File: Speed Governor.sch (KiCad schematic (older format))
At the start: 11 parts

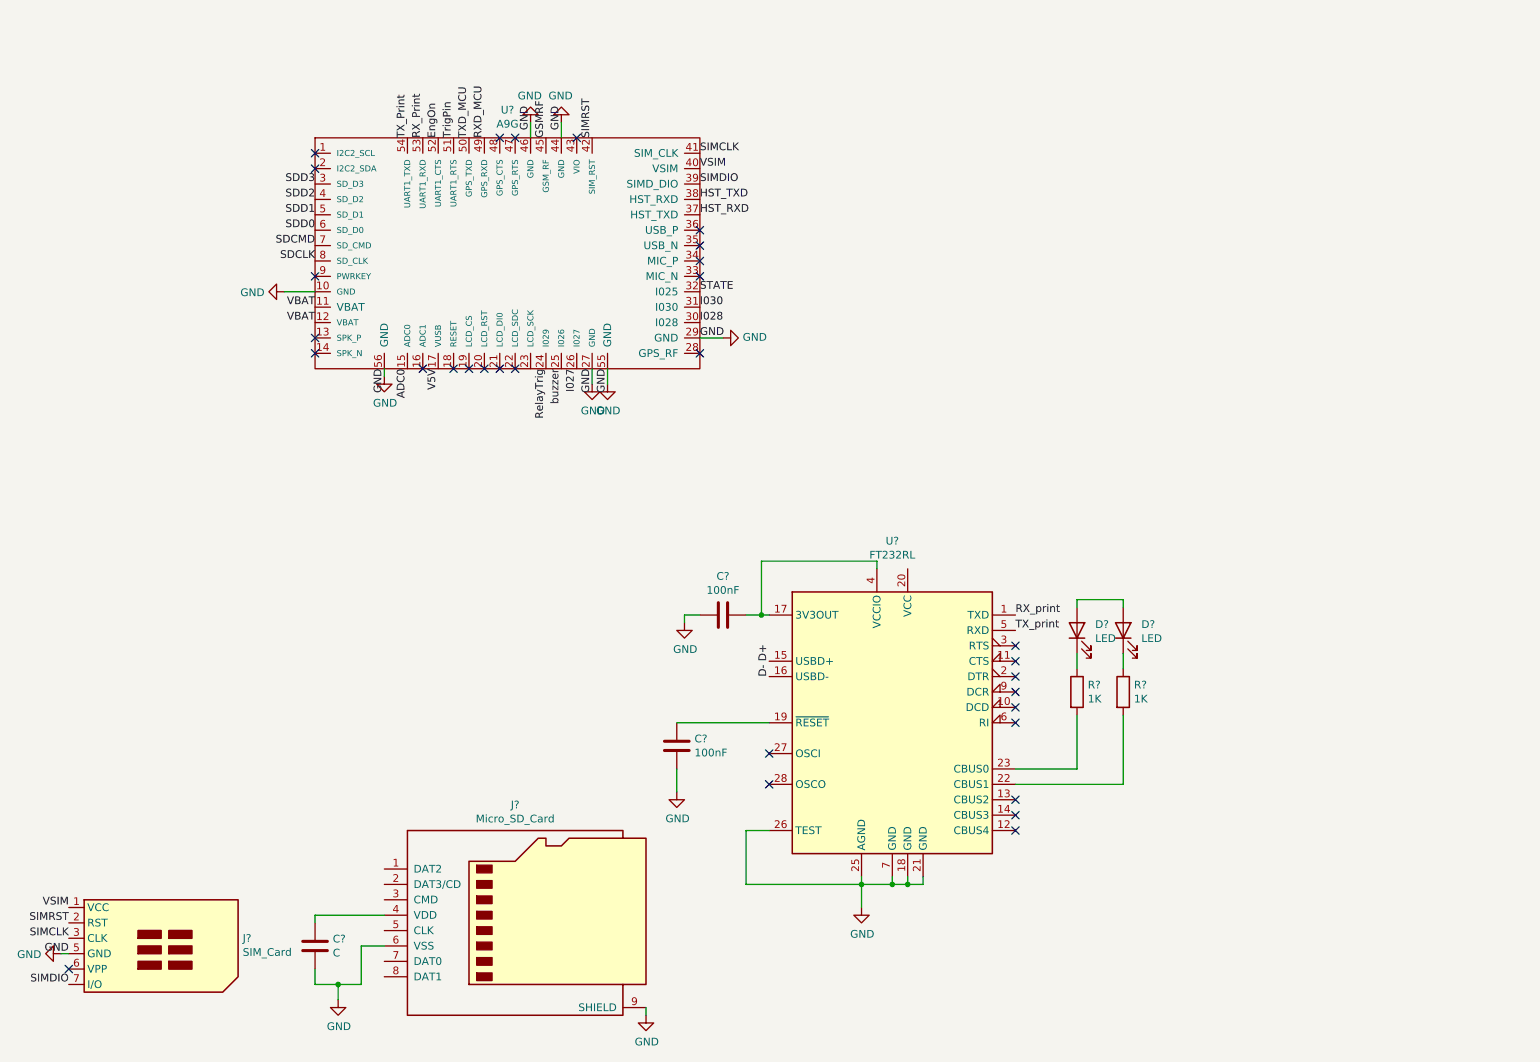
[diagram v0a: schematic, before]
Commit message: added schematic symbols and other libraries
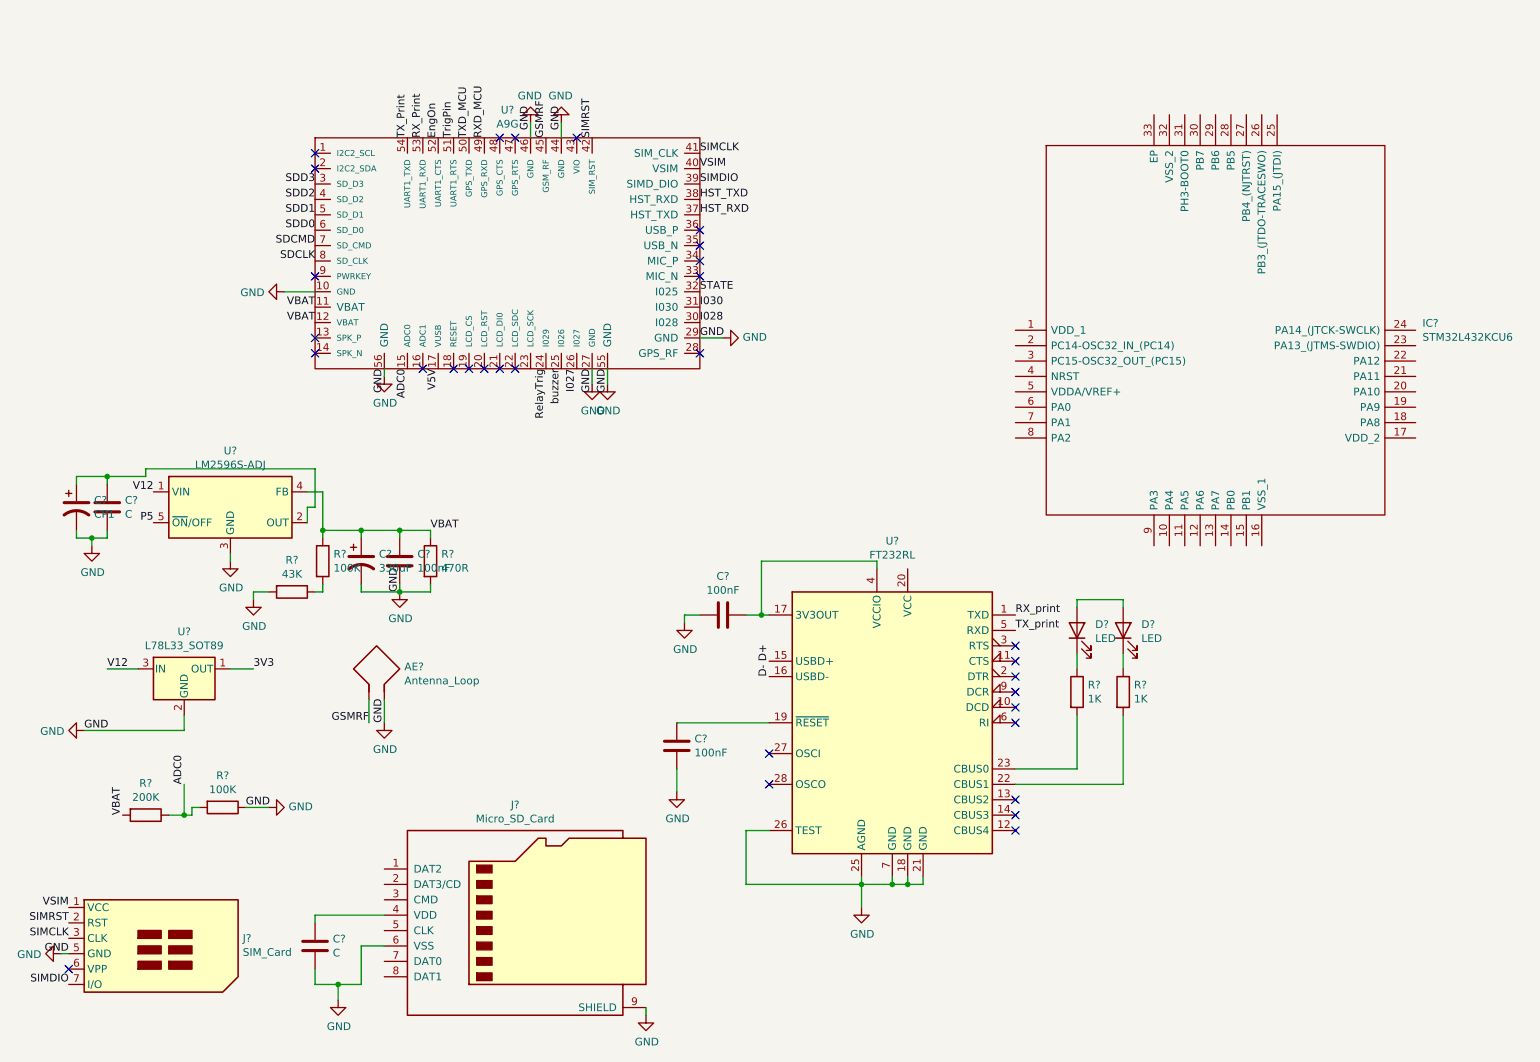
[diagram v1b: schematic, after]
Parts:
- added AE?: Antenna_Loop, symbol Device:Antenna_Loop
- added C?: 330uF, symbol Device:CP1
- added C?: 100nF, symbol Device:C
- added C?: CP1, symbol Device:CP1
- added C?: C, symbol Device:C
- added IC?: STM32L432KCU6, QFN50P500X500X60-33N-D, symbol STM32L432KCU6:STM32L432KCU6
- added R?: 200K, symbol Device:R
- added R? (x2): 100K, symbol Device:R
- added R?: 470R, symbol Device:R
- added R?: 43K, symbol Device:R
- added U?: L78L33_SOT89, Package_TO_SOT_SMD:SOT-89-3, symbol Regulator_Linear:L78L33_SOT89
- added U?: LM2596S-ADJ, Package_TO_SOT_SMD:TO-263-5_TabPin3, symbol Regulator_Switching:LM2596S-ADJ
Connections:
- net ADC0: now also R?.1, R?.2
- net GND: now also AE?.2, C?.2, C?.2, C?.2, C?.2, R?.1, R?.2, R?.2, U?.2 (GND), U?.3 (GND)
- net GSMRF: now also AE?.1
- net VBAT: now also C?.1, C?.1, R?.1, R?.1, R?.2, U?.4 (FB)
- new net: C?.1, C?.1, U?.2 (OUT)
- new net: R?.1, R?.2
- new net 3V3: U?.1 (OUT)
- new net P5: U?.5 (~ON~/OFF)
- new net V12: U?.1 (VIN), U?.3 (IN)

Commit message: added SIM 808
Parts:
- removed IC?: STM32L432KCU6, QFN50P500X500X60-33N-D, symbol STM32L432KCU6:STM32L432KCU6
- added U?: SIM808, XCVR_SIM808, symbol SIM808:SIM808
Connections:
- new net: U?.1 (GND), U?.18 (GND), U?.2 (GND), U?.28 (GND), U?.3 (GND), U?.34 (GND), U?.36 (GND), U?.40 (GND), U?.51 (GND), U?.52 (GND), U?.54 (GND), U?.64 (GND), U?.65 (GND), U?.67 (GND), U?.68 (GND)
- new net: U?.4 (VBAT), U?.5 (VBAT), U?.6 (VBAT)
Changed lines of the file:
@@
 GND
 $Comp
-L STM32L432KCU6:STM32L432KCU6 IC?
-U 1 1 6038E929
-P 6950 3100
-F 0 "IC?" H 9594 3146 50  0000 L CNN
-F 1 "STM32L432KCU6" H 9594 3055 50  0000 L CNN
-F 2 "QFN50P500X500X60-33N-D" H 9400 4300 50  0001 L CNN
-F 3 "http://www.st.com/content/ccc/resource/technical/document/datasheet/24/01/9f/59/f0/83/47/fc/DM00257205.pdf/files/DM00257205.pdf/jcr:content/translations/en.DM00257205.pdf" H 9400 4200 50  0001 L CNN
-F 4 "STMICROELECTRONICS - STM32L432KCU6 - MCU, ARM CORTEX-M4, 80MHZ, UFQFPN-32" H 9400 4100 50  0001 L CNN "Description"
-F 5 "0.6" H 9400 4000 50  0001 L CNN "Height"
-F 6 "STMicroelectronics" H 9400 3900 50  0001 L CNN "Manufacturer_Name"
-F 7 "STM32L432KCU6" H 9400 3800 50  0001 L CNN "Manufacturer_Part_Number"
-F 8 "511-STM32L432KCU6" H 9400 3700 50  0001 L CNN "Mouser Part Number"
-F 9 "https://www.mouser.co.uk/ProductDetail/STMicroelectronics/STM32L432KCU6?qs=dTJS0cRn7oiybcTRwI97Tw%3D%3D" H 9400 3600 50  0001 L CNN "Mouser Price/Stock"
-F 10 "STM32L432KCU6" H 9400 3500 50  0001 L CNN "Arrow Part Number"
-F 11 "https://www.arrow.com/en/products/stm32l432kcu6/stmicroelectronics" H 9400 3400 50  0001 L CNN "Arrow Price/Stock"
-	1    6950 3100
+L SIM808:SIM808 U?
+U 1 1 602DB42F
+P 7900 3150
+F 0 "U?" H 7900 5215 50  0000 C CNN
+F 1 "SIM808" H 7900 5124 50  0000 C CNN
+F 2 "XCVR_SIM808" H 7900 3150 50  0001 L BNN
+F 3 "" H 7900 3150 50  0001 L BNN
+F 4 "SIMCOM" H 7900 3150 50  0001 L BNN "MANUFACTURER"
+F 5 "2.8mm" H 7900 3150 50  0001 L BNN "MAXIMUM_PACKAGE_HEIGHT"
+F 6 "Manufacturer recommendations" H 7900 3150 50  0001 L BNN "STANDARD"
+F 7 "1.03" H 7900 3150 50  0001 L BNN "PARTREV"
+	1    7900 3150
 	1    0    0    -1
 $EndComp
